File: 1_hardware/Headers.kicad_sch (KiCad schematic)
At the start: 17 parts, among them J111 SSW-132-24-L-D, J121 SSW-132-24-L-D, J2 Power, J3 Buttons, J4 Reserve2

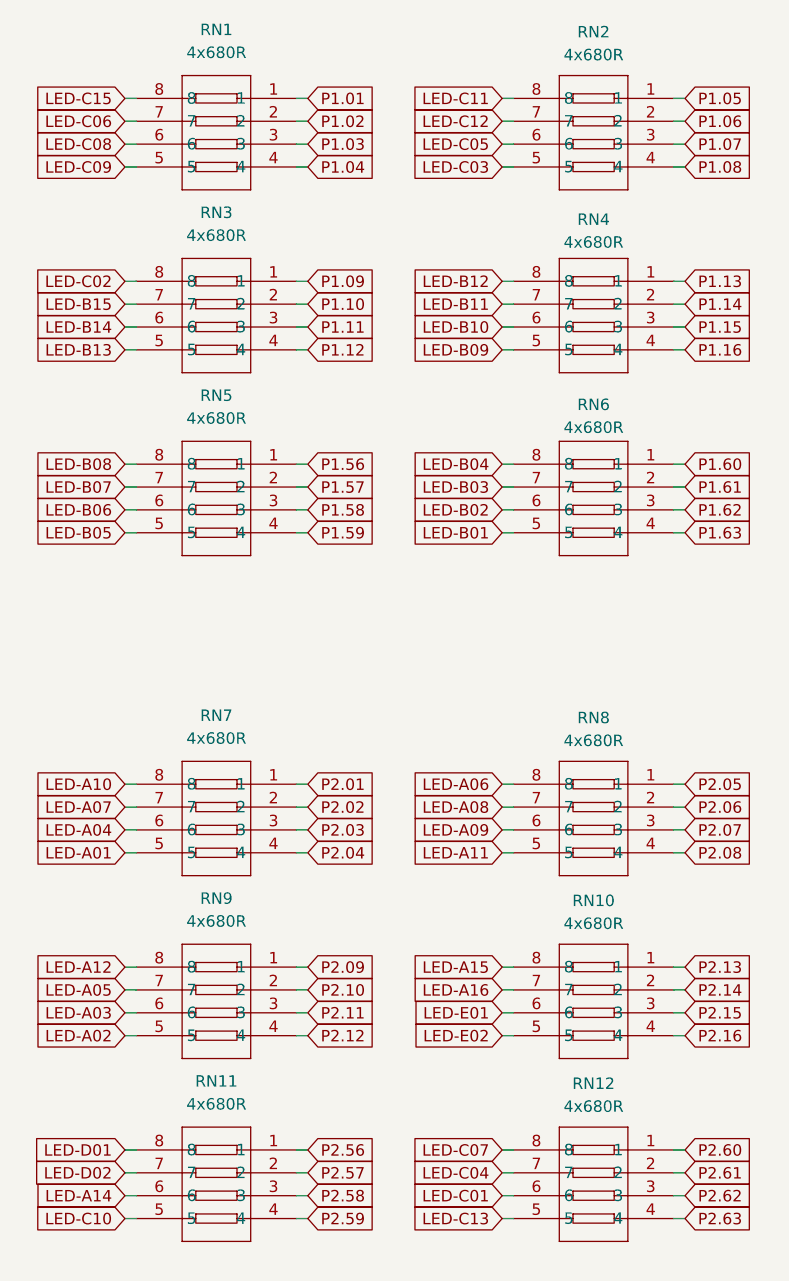
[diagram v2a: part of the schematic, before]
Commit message: changed from STM32F103C8 over to STM32L151C8 changed controller pinout, minor tweaks in board design, added labels and debug pads
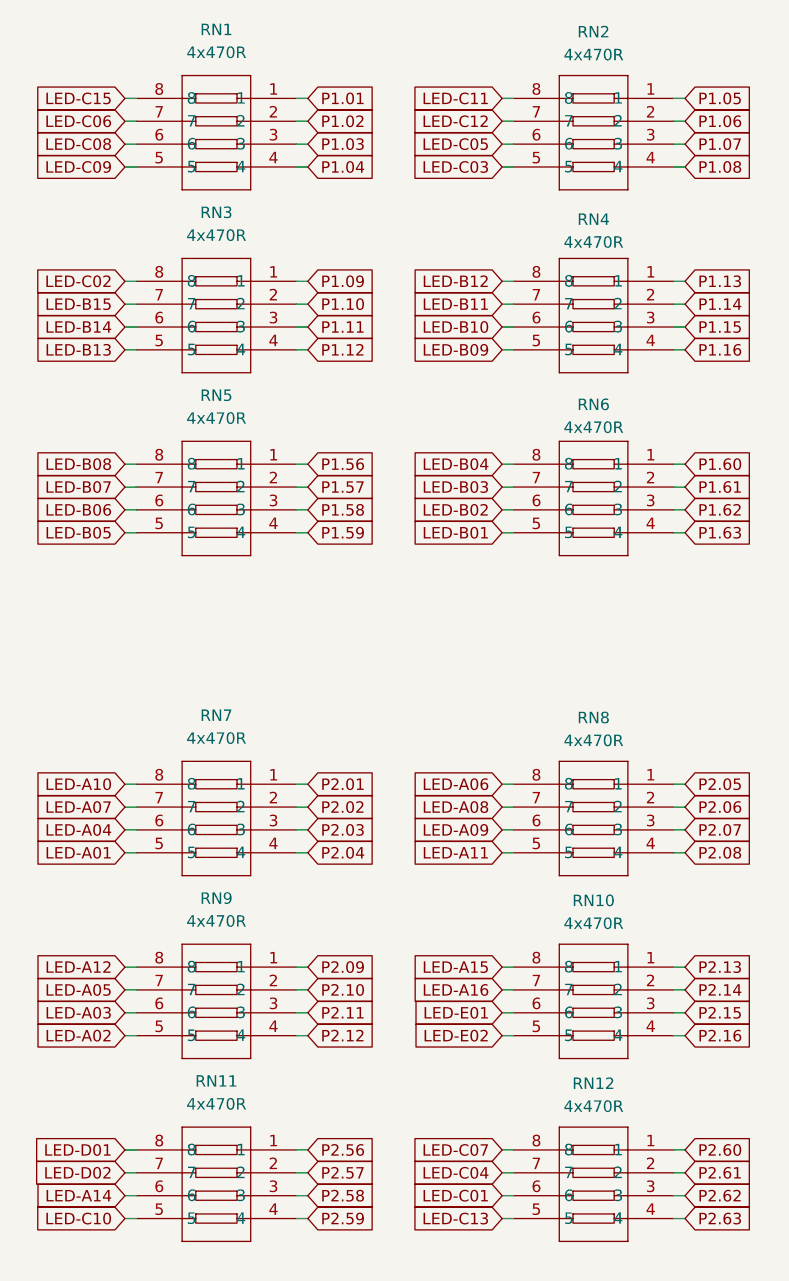
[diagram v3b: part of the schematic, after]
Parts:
- RN1, RN10, RN11, RN12, RN2, RN3, RN4, RN5, RN6, RN7, RN8, RN9: value 4x680R -> 4x470R; LCSC Part C12035 -> C25510
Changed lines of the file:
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@@
 			)
 		)
-		(property "Value" "4x680R"
+		(property "Value" "4x470R"
 			(at 208.28 95.25 0)
 			(effects
@@
 			)
 		)
-		(property "Datasheet" "https://lcsc.com/product-detail/Resistor-Networks-Arrays_680R-681-5_C12035.html"
+		(property "Datasheet" "https://www.lcsc.com/product-detail/Resistor-Networks-Arrays_UNI-ROYAL-Uniroyal-Elec-4D03WGJ0471T5E_C25510.html"
 			(at 208.28 118.11 0)
 			(effects
@@
 			)
 		)
-		(property "LCSC Part" "C12035"
+		(property "LCSC Part" "C25510"
 			(at 208.28 120.65 0)
 			(effects
@@
 			)
 		)
-		(property "Value" "4x680R"
+		(property "Value" "4x470R"
 			(at 250.19 115.824 0)
 			(effects
@@
 			)
 		)
-		(property "Datasheet" "https://lcsc.com/product-detail/Resistor-Networks-Arrays_680R-681-5_C12035.html"
+		(property "Datasheet" "https://www.lcsc.com/product-detail/Resistor-Networks-Arrays_UNI-ROYAL-Uniroyal-Elec-4D03WGJ0471T5E_C25510.html"
 			(at 250.19 138.43 0)
 			(effects
@@
 			)
 		)
-		(property "LCSC Part" "C12035"
+		(property "LCSC Part" "C25510"
 			(at 250.19 140.97 0)
 			(effects
@@
 			)
 		)
-		(property "Value" "4x680R"
+		(property "Value" "4x470R"
 			(at 250.19 136.144 0)
 			(effects
@@
 			)
 		)
-		(property "Datasheet" "https://lcsc.com/product-detail/Resistor-Networks-Arrays_680R-681-5_C12035.html"
+		(property "Datasheet" "https://www.lcsc.com/product-detail/Resistor-Networks-Arrays_UNI-ROYAL-Uniroyal-Elec-4D03WGJ0471T5E_C25510.html"
 			(at 250.19 158.75 0)
 			(effects
@@
 			)
 		)
-		(property "LCSC Part" "C12035"
+		(property "LCSC Part" "C25510"
 			(at 250.19 161.29 0)
 			(effects
@@
 			)
 		)
-		(property "Value" "4x680R"
+		(property "Value" "4x470R"
 			(at 208.28 115.57 0)
 			(effects
@@
 			)
 		)
-		(property "Datasheet" "https://lcsc.com/product-detail/Resistor-Networks-Arrays_680R-681-5_C12035.html"
+		(property "Datasheet" "https://www.lcsc.com/product-detail/Resistor-Networks-Arrays_UNI-ROYAL-Uniroyal-Elec-4D03WGJ0471T5E_C25510.html"
 			(at 208.28 138.43 0)
 			(effects
@@
 			)
 		)
-		(property "LCSC Part" "C12035"
+		(property "LCSC Part" "C25510"
 			(at 208.28 140.97 0)
 			(effects
@@
 			)
 		)
-		(property "Value" "4x680R"
+		(property "Value" "4x470R"
 			(at 250.19 95.504 0)
 			(effects
@@
 			)
 		)
-		(property "Datasheet" "https://lcsc.com/product-detail/Resistor-Networks-Arrays_680R-681-5_C12035.html"
+		(property "Datasheet" "https://www.lcsc.com/product-detail/Resistor-Networks-Arrays_UNI-ROYAL-Uniroyal-Elec-4D03WGJ0471T5E_C25510.html"
 			(at 250.19 118.11 0)
 			(effects
@@
 			)
 		)
-		(property "LCSC Part" "C12035"
+		(property "LCSC Part" "C25510"
 			(at 250.19 120.65 0)
 			(effects
@@
 			)
 		)
-		(property "Value" "4x680R"
+		(property "Value" "4x470R"
 			(at 250.19 60.706 0)
 			(effects
@@
 			)
 		)
-		(property "Datasheet" "https://lcsc.com/product-detail/Resistor-Networks-Arrays_680R-681-5_C12035.html"
+		(property "Datasheet" "https://www.lcsc.com/product-detail/Resistor-Networks-Arrays_UNI-ROYAL-Uniroyal-Elec-4D03WGJ0471T5E_C25510.html"
 			(at 250.19 82.55 0)
 			(effects
@@
 			)
 		)
-		(property "LCSC Part" "C12035"
+		(property "LCSC Part" "C25510"
 			(at 250.19 85.09 0)
 			(effects
@@
 			)
 		)
-		(property "Value" "4x680R"
+		(property "Value" "4x470R"
 			(at 208.28 135.89 0)
 			(effects
@@
 			)
 		)
-		(property "Datasheet" "https://lcsc.com/product-detail/Resistor-Networks-Arrays_680R-681-5_C12035.html"
+		(property "Datasheet" "https://www.lcsc.com/product-detail/Resistor-Networks-Arrays_UNI-ROYAL-Uniroyal-Elec-4D03WGJ0471T5E_C25510.html"
 			(at 208.28 158.75 0)
 			(effects
@@
 			)
 		)
-		(property "LCSC Part" "C12035"
+		(property "LCSC Part" "C25510"
 			(at 208.28 161.29 0)
 			(effects
@@
 			)
 		)
-		(property "Value" "4x680R"
+		(property "Value" "4x470R"
 			(at 250.19 19.304 0)
 			(effects
@@
 			)
 		)
-		(property "Datasheet" "https://lcsc.com/product-detail/Resistor-Networks-Arrays_680R-681-5_C12035.html"
+		(property "Datasheet" "https://www.lcsc.com/product-detail/Resistor-Networks-Arrays_UNI-ROYAL-Uniroyal-Elec-4D03WGJ0471T5E_C25510.html"
 			(at 250.19 41.91 0)
 			(effects
@@
 			)
 		)
-		(property "LCSC Part" "C12035"
+		(property "LCSC Part" "C25510"
 			(at 250.19 44.45 0)
 			(effects
@@
 			)
 		)
-		(property "Value" "4x680R"
+		(property "Value" "4x470R"
 			(at 208.28 19.05 0)
 			(effects
@@
 			)
 		)
-		(property "Datasheet" "https://lcsc.com/product-detail/Resistor-Networks-Arrays_680R-681-5_C12035.html"
+		(property "Datasheet" "https://www.lcsc.com/product-detail/Resistor-Networks-Arrays_UNI-ROYAL-Uniroyal-Elec-4D03WGJ0471T5E_C25510.html"
 			(at 208.28 41.91 0)
 			(effects
@@
 			)
 		)
-		(property "LCSC Part" "C12035"
+		(property "LCSC Part" "C25510"
 			(at 208.28 44.45 0)
 			(effects
@@
 			)
 		)
-		(property "Value" "4x680R"
+		(property "Value" "4x470R"
 			(at 208.28 39.37 0)
 			(effects
@@
 			)
 		)
-		(property "Datasheet" "https://lcsc.com/product-detail/Resistor-Networks-Arrays_680R-681-5_C12035.html"
+		(property "Datasheet" "https://www.lcsc.com/product-detail/Resistor-Networks-Arrays_UNI-ROYAL-Uniroyal-Elec-4D03WGJ0471T5E_C25510.html"
 			(at 208.28 62.23 0)
 			(effects
@@
 			)
 		)
-		(property "LCSC Part" "C12035"
+		(property "LCSC Part" "C25510"
 			(at 208.28 64.77 0)
 			(effects
@@
 			)
 		)
-		(property "Value" "4x680R"
+		(property "Value" "4x470R"
 			(at 250.19 40.132 0)
 			(effects
@@
 			)
 		)
-		(property "Datasheet" "https://lcsc.com/product-detail/Resistor-Networks-Arrays_680R-681-5_C12035.html"
+		(property "Datasheet" "https://www.lcsc.com/product-detail/Resistor-Networks-Arrays_UNI-ROYAL-Uniroyal-Elec-4D03WGJ0471T5E_C25510.html"
 			(at 250.19 62.23 0)
 			(effects
@@
 			)
 		)
-		(property "LCSC Part" "C12035"
+		(property "LCSC Part" "C25510"
 			(at 250.19 64.77 0)
 			(effects
@@
 			)
 		)
-		(property "Value" "4x680R"
+		(property "Value" "4x470R"
 			(at 208.28 59.69 0)
 			(effects
@@
 			)
 		)
-		(property "Datasheet" "https://lcsc.com/product-detail/Resistor-Networks-Arrays_680R-681-5_C12035.html"
+		(property "Datasheet" "https://www.lcsc.com/product-detail/Resistor-Networks-Arrays_UNI-ROYAL-Uniroyal-Elec-4D03WGJ0471T5E_C25510.html"
 			(at 208.28 82.55 0)
 			(effects
@@
 			)
 		)
-		(property "LCSC Part" "C12035"
+		(property "LCSC Part" "C25510"
 			(at 208.28 85.09 0)
 			(effects

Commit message: finished v0.9.2
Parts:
- RN1, RN10, RN11, RN12, RN2, RN3, RN4, RN5, RN6, RN7, RN8, RN9: value 4x470R -> 4x680R
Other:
- note added: "J111 LEDs Resistor-Networks"
- note added: "J121 LEDs Resistor-Networks"
- note added: "PinHeader"
- note added: "Terminal blocks"
- moved on the sheet: J2, J3, J4

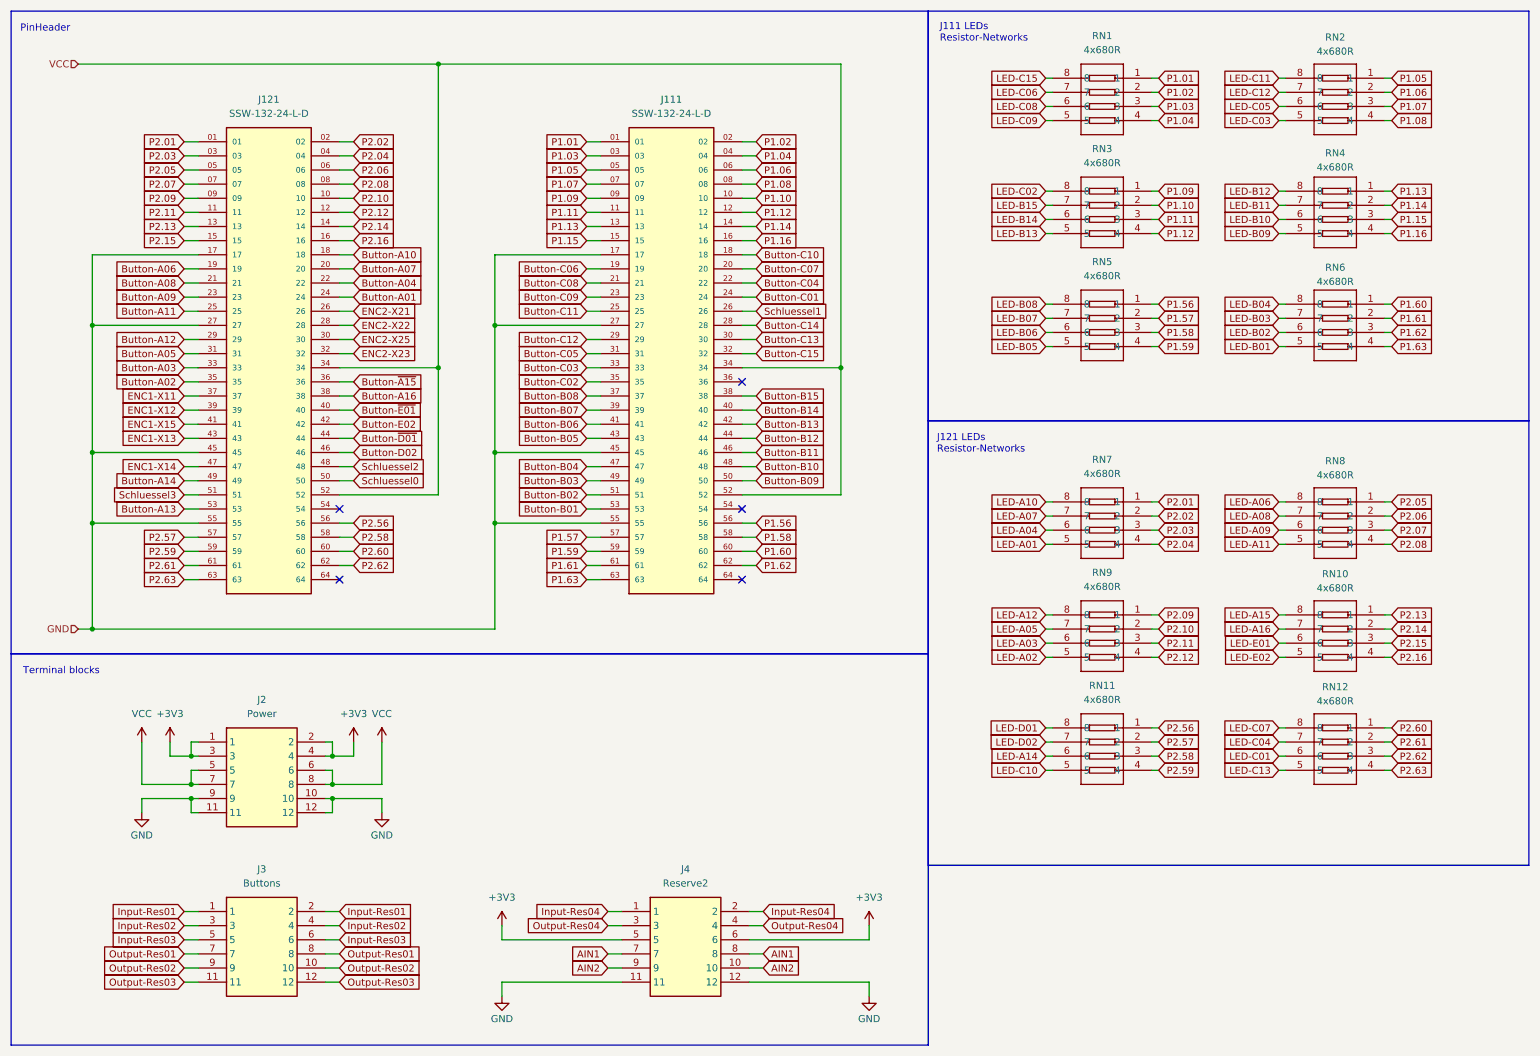
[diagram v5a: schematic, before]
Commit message: PCB v0.9.4 - finished final prototype STM32 project reinitialised (F103C8 -> L151C8)
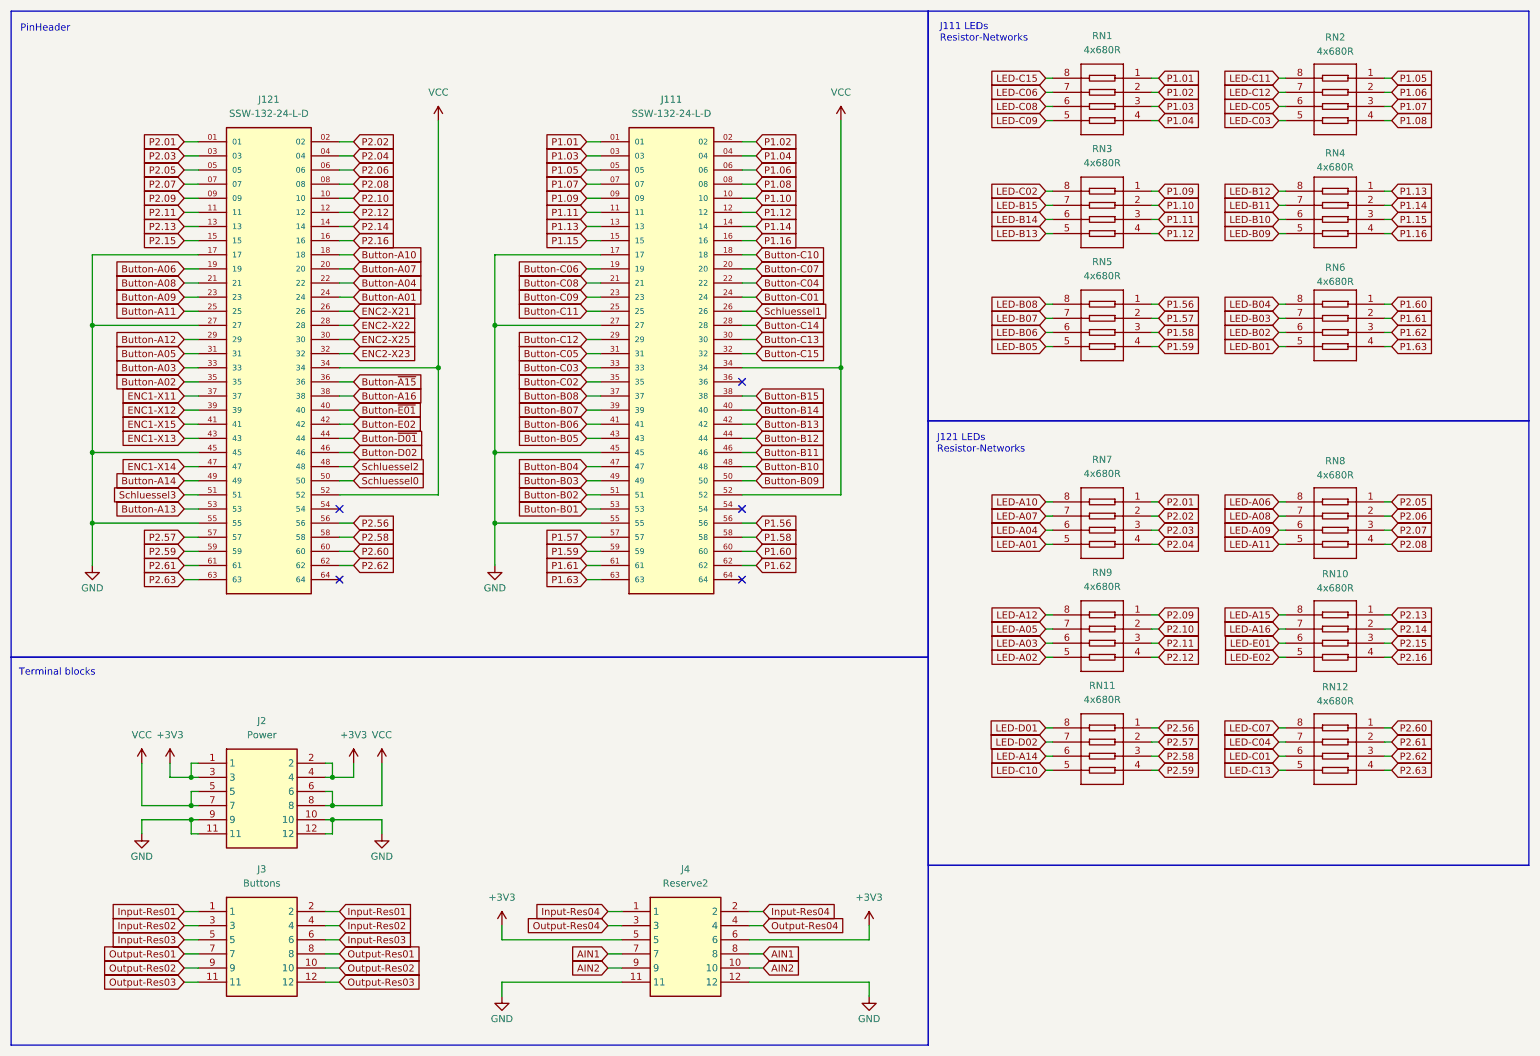
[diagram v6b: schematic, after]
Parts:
- J111, J121: footprint CostumLibrary:SAMTEC_SSW-132-24-L-D -> project_library:SAMTEC_SSW-132-24-L-D; symbol CostumLibrary:SSW-132-24-L-D -> project_library:SSW-132-24-L-D
- J2, J3, J4: footprint CostumLibrary:1824460000 - LSF-SMT 3.500690 3.5SN BK TU -> project_library:1824460000 - LSF-SMT 3.500690 3.5SN BK TU; symbol CostumLibrary:1824460000 - LSF-SMT 3.50/06/90 3.5SN BK TU -> project_library:1824460000 - LSF-SMT 3.50/06/90 3.5SN BK TU
- RN1, RN10, RN11, RN12, RN2, RN3, RN4, RN5, RN6, RN7, RN8, RN9: footprint easyeda2kicad:RES-ARRAY-SMD_0603-8P-L3.2-W1.6-BL -> project_library:RES-ARRAY-SMD_0603-8P-L3.2-W1.6-BL; symbol easyeda2kicad:4D03WGJ0681T5E -> project_library:4D03WGJ0681T5E; LCSC Part C25510 -> C12035
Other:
- moved on the sheet: J2
